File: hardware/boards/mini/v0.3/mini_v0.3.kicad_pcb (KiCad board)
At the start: 8 copper layers, 20 x 40 mm, 95 parts, among them IC1 NAU88C22YG, IC3 IS42S16160J-6BLI, J1 Connector, U1 W25Q128JVP, U2 LTV-217-G, U4 STM32H750XBHx, Y1 Crystal_GND24, Y3 32.768kHz

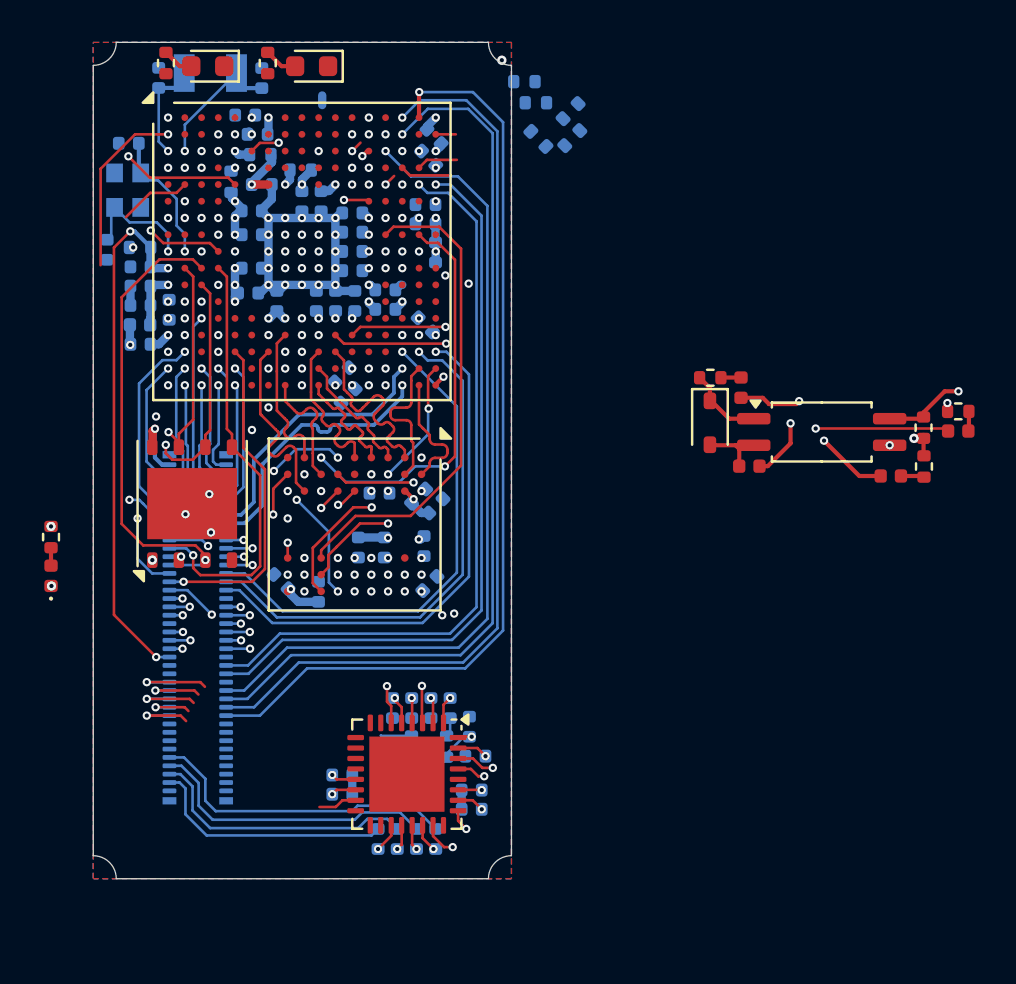
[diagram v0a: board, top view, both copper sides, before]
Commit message: mini: use 90-pin port instead of 80
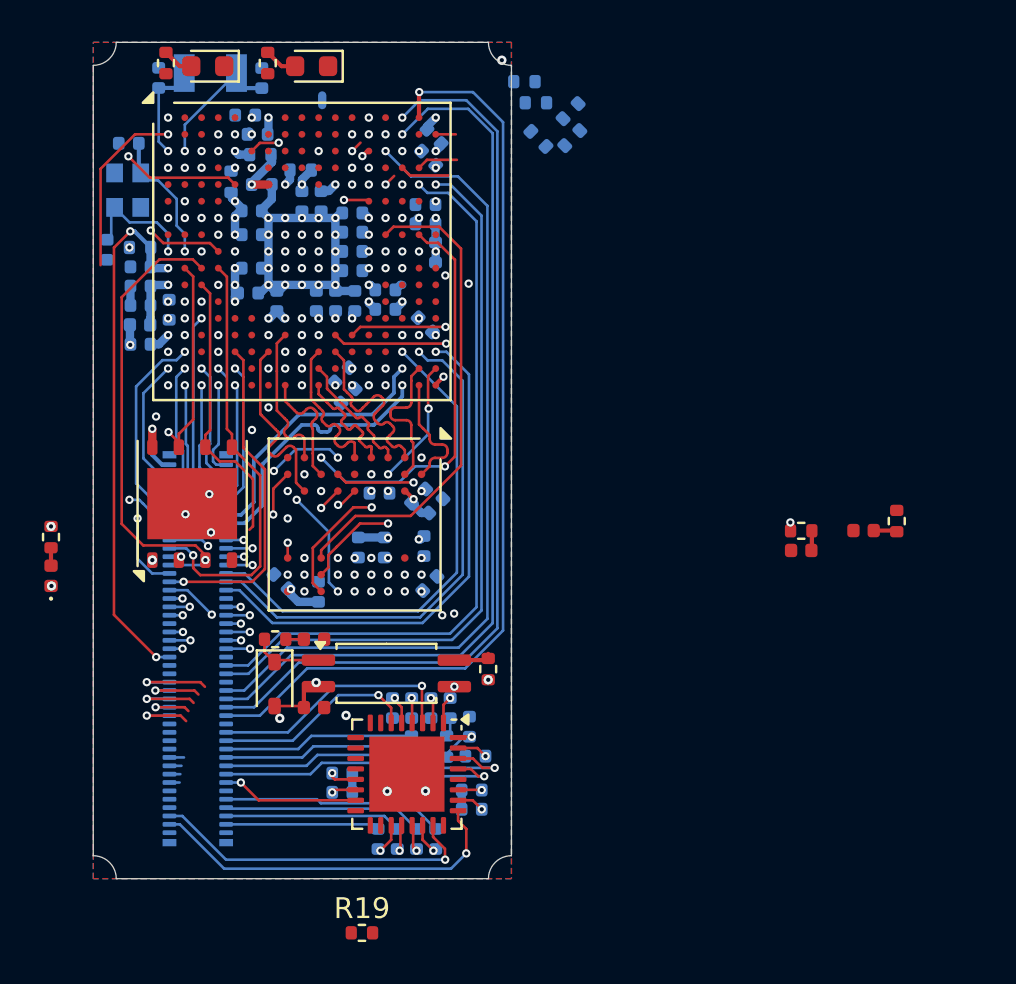
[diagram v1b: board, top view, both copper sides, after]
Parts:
- removed J1: Connector, Connector_Hirose_DF40:Hirose_DF40C-80DP-0.4V_2x40-1MP_P0.4mm
- added J4: DF40C-90DP-0.4V, Connector_Hirose_DF40:Hirose_DF40C-90DP-0.4V_2x45-1MP_P0.4mm, B.Cu at (75.0, 86.0)
- added R19: 10k, Resistor_SMD:R_0402_1005Metric, F.Cu at (82.8, 99.6)
- moved D3 24.3 mm to (78.7, 87.7)
- moved R7 24.3 mm to (78.7, 85.5)
- moved U2 23.8 mm to (84.0, 87.2)
- moved FB3 23.8 mm to (80.6, 88.8)
- moved R6 23.8 mm to (88.9, 87.0)
- moved FB2 23.7 mm to (80.6, 85.5), turned to 180 degrees
- moved FB4 9.43 mm to (103.9, 81.3)
- moved R8 9.43 mm to (103.9, 80.4)
- moved R9 2.92 mm to (108.4, 79.9)
- moved FB5 2.92 mm to (106.8, 80.3)
- moved C17 0.09 mm to (81.9, 92.0)
- moved C16 0.09 mm to (81.9, 92.9)
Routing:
- net /SPKL: track 1.03 -> 17.6 mm
- net /SPKR: track 1.67 -> 15.9 mm
- net /HPL: track 1.85 -> 15.3 mm
- net /HPR: track 1.39 -> 14.2 mm
- net /LIN: track 1.82 -> 12.1 mm
- net /MICR: track 2.33 -> 10.4 mm
- net /RIN: track 1.85 -> 9.77 mm
- net /MICL: track 4.18 -> 11.9 mm
- net /DIN_OUT_SINK: track 6.38 -> 0.17 mm, vias 1 -> 0
- net /CODEC_GPIO: track 1.86 -> 6.55 mm, vias 0 -> 1
- net /AUX_IN_R: track 13.0 -> 8.44 mm
- net /AUX_IN_L: track 11.9 -> 7.36 mm
- net /AUX_OUT_L: track 14.0 -> 9.53 mm
- net /AUX_OUT_R: track 15.0 -> 10.6 mm
- net /LED_STATUS2: track 3.47 -> 0.00 mm
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
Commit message: mini: various routing tweaks
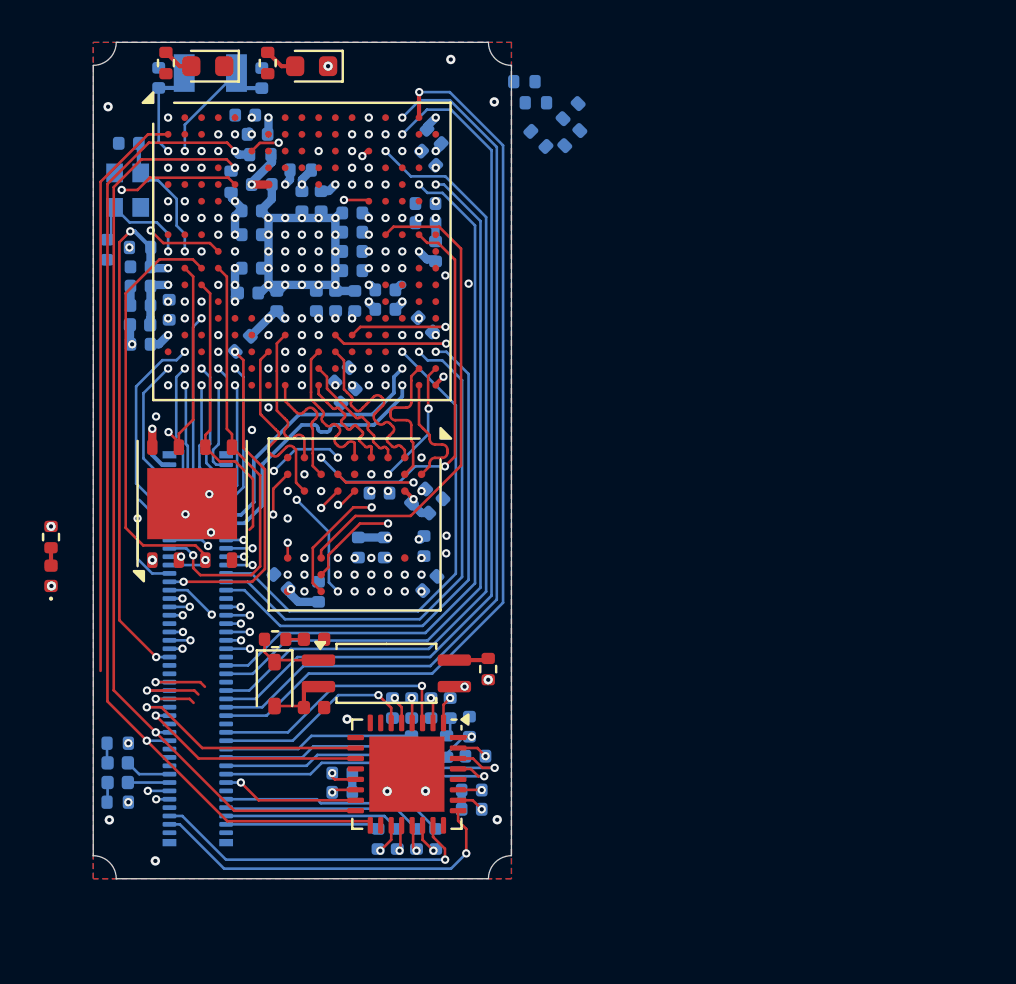
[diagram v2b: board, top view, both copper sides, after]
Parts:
- FB4, FB5, R19, R8, R9: moved to B.Cu
- moved R9 38.7 mm to (71.2, 90.5), turned to 0 degrees
- moved FB5 37.4 mm to (71.2, 91.5), turned to 0 degrees
- moved R8 35.2 mm to (71.2, 93.3), turned to 180 degrees
- moved FB4 34.5 mm to (71.2, 92.4), turned to 0 degrees
- moved R19 28.7 mm to (77.2, 71.4), turned to -135 degrees
- moved C4 0.05 mm to (85.9, 64.7)
- moved C5 0.05 mm to (85.9, 65.6)
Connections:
- J4 pad 59: /SAI1_MCLK -> /SAI1_SD_A
- J4 pad 61: /SAI1_SD_A -> /SAI1_MCLK
- J4 pad 63: unconnected-(J4-Pad63) -> GND
- J4 pad 65: unconnected-(J4-Pad65) -> /I2C_SCL
- J4 pad 67: unconnected-(J4-Pad67) -> /I2C_SDA
- J4 pad 73: unconnected-(J4-Pad73) -> GND
- J4 pad 75: unconnected-(J4-Pad75) -> /DIN_OUT_SOURCE
- J4 pad 77: unconnected-(J4-Pad77) -> /DIN_OUT_SINK
- J4 pad 79: unconnected-(J4-Pad79) -> /DIN_IN_SOURCE
- J4 pad 81: unconnected-(J4-Pad81) -> /DIN_IN_SINK
- J4 pad 83: unconnected-(J4-Pad83) -> GND
- U4 pad E2: /LED_STATUS2 -> unconnected-(U4I-PI9-PadE2)
- U4 pad H15: /EXT_QSPI_DETECT -> unconnected-(U4G-PG3-PadH15)
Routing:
- net /I2C_SDA: track 4.79 -> 49.0 mm, vias 1 -> 2
- net /I2C_SCL: track 5.60 -> 45.4 mm, vias 1 -> 2
- net /VBAT: track 8.52 -> 27.6 mm, vias 1 -> 0
- net /SAI1_MCLK: track 34.0 -> 43.7 mm
- net /SAI1_SD_A: track 37.4 -> 44.3 mm
- net /BOOT0: track 6.05 -> 0.79 mm
- net /DIN_MIDI_TX: track 19.9 -> 14.9 mm
- net /DIN_MIDI_RX: track 21.9 -> 18.6 mm
- net /PA9: track 2.48 -> 0.00 mm
- net /DIN_OUT_SOURCE: track 0.00 -> 2.21 mm
- net /PH13: track 1.97 -> 0.00 mm
- net /DIN_OUT_SINK: track 0.17 -> 2.03 mm
- net /SPI_NSS: track 45.1 -> 43.6 mm
- net /SPI_MISO: track 43.0 -> 41.6 mm
- net /SPI_SCK: track 43.8 -> 42.5 mm
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
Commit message: mini: various routing adjustments
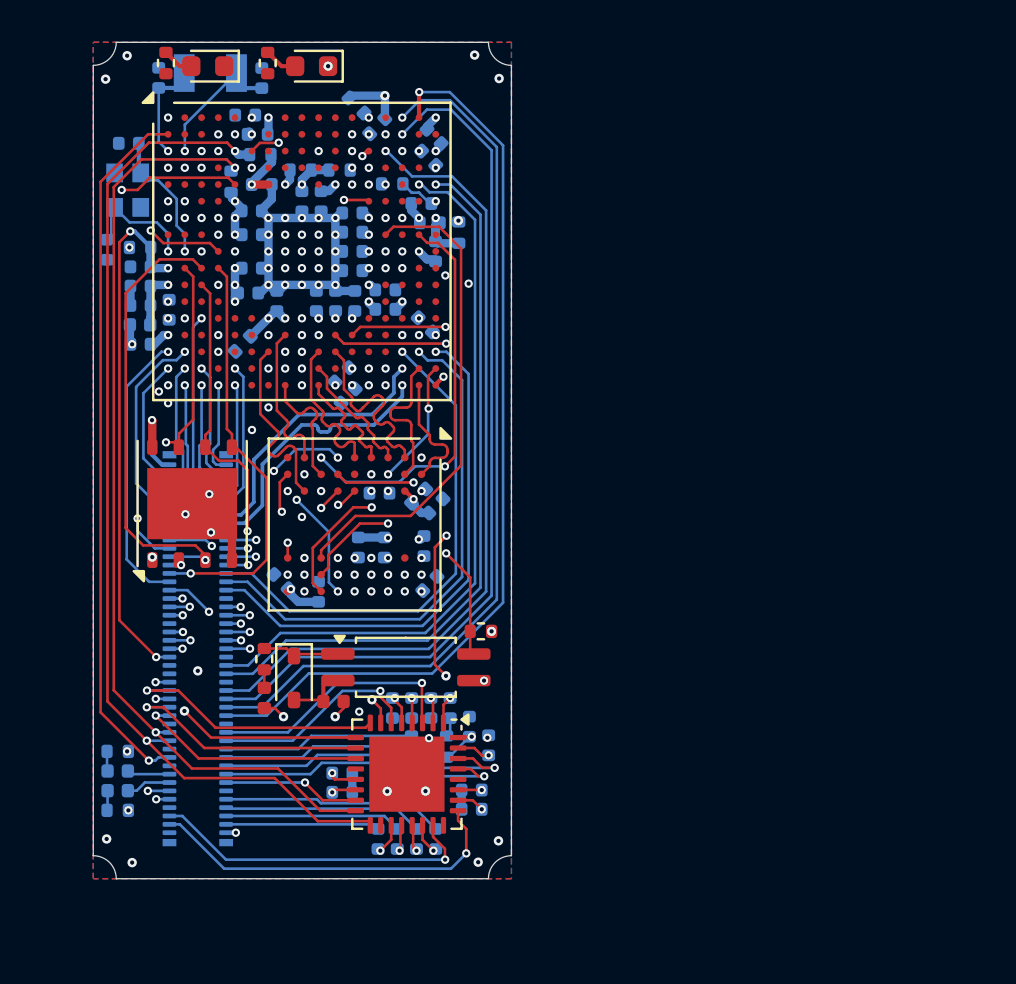
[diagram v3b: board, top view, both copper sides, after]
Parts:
- removed D1: POWER, LED_SMD:LED_0402_1005Metric
- removed R16: R, Resistor_SMD:R_0402_1005Metric
- moved R10 9.80 mm to (81.8, 63.1)
- moved R14 9.28 mm to (83.6, 61.0)
- moved R12 8.88 mm to (84.3, 63.8), turned to 180 degrees
- moved R13 8.58 mm to (82.6, 60.0), turned to -45 degrees
- moved R11 5.88 mm to (87.5, 66.1), turned to 90 degrees
- moved FB2 3.68 mm to (78.2, 88.4), turned to 90 degrees
- moved R9 3.21 mm to (71.2, 93.7)
- moved R8 2.43 mm to (71.2, 90.9)
- moved R6 1.84 mm to (88.5, 85.2), turned to 180 degrees
- moved FB5 1.33 mm to (71.2, 92.8)
- moved R7 1.08 mm to (78.2, 86.5), turned to 90 degrees
- moved U2 0.97 mm to (85.0, 86.9)
- moved D3 0.97 mm to (79.6, 87.4)
- moved FB3 0.97 mm to (81.5, 88.5)
- moved C19 0.82 mm to (88.9, 90.6), turned to 90 degrees
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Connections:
- J4 pad 17: unconnected-(J4-Pad17) -> GND
- J4 pad 21: /QSPI_IO0 -> /QSPI_IO3
- J4 pad 23: /QSPI_IO1 -> /QSPI_IO2
- J4 pad 25: /QSPI_IO2 -> /QSPI_IO1
- J4 pad 27: /QSPI_IO3 -> /QSPI_IO0
- J4 pad 29: /EXT_QSPI_DETECT -> /PC2_C
- J4 pad 69: unconnected-(J4-Pad69) -> GND
- J4 pad 71: unconnected-(J4-Pad71) -> /VBAT
- J4 pad 75: /DIN_OUT_SOURCE -> /DIN_OUT_SINK
- J4 pad 77: /DIN_OUT_SINK -> /DIN_OUT_SOURCE
- R19 pad 2: /EXT_QSPI_DETECT -> /PC2_C
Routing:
- net /DIN_MIDI_TX: track 14.9 -> 38.8 mm, vias 3 -> 4
- net /EXT_QSPI_DETECT: track 15.8 -> 0.00 mm, vias 2 -> 0
- net /PC2_C: track 0.00 -> 13.4 mm, vias 0 -> 1
- net /DIN_IN_SINK: track 0.63 -> 11.7 mm, vias 1 -> 2
- net +3.3V: track 44.2 -> 54.9 mm, vias 42 -> 43
- net /SAI1_FS: track 31.9 -> 41.6 mm, vias 2 -> 3
- net /DIN_IN_SOURCE: track 1.03 -> 10.1 mm, vias 1 -> 2
- net /SAI1_SCK: track 30.4 -> 39.3 mm
- net /SAI1_SD_B: track 31.0 -> 38.9 mm, vias 2 -> 3
- net /VBAT: track 27.6 -> 33.9 mm, vias 0 -> 1
- net /PC2: track 4.47 -> 0.00 mm, vias 1 -> 0
- net GND: track 31.4 -> 35.6 mm, vias 69 -> 73
- net /PC1: track 3.63 -> 0.00 mm, vias 1 -> 0
- net /DIN_MIDI_RX: track 18.6 -> 21.3 mm
- net /QSPI_CLK: track 15.4 -> 17.7 mm, vias 1 -> 2
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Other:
- board text added: "USB differential pair is impedance matched assuming JLC08161H-2116 stackup which is {dblquote}free{dblquote} for 8-layer boards. JLC impedance tool gives: Trace width: 0.1773mil Trace spacing: 0.2mm"
- board text removed: "USB differential pair is impedance matches assuming JLC08161H-2116 stackup which is {dblquote}free{dblquote} for 8-layer boards. JLC impedance tool gives: Trace width: 0.1773mil Trace spacing: 0.2mm"
